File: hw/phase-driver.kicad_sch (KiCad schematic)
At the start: 13 parts, among them IC401 SN74AHCT1G125DRLR, IC402 SN74AHCT1G125DRLR, IC403 SN74AHCT1G125DRLR, Q401 MMBF170, Q402 MMBF170, Q403 MMBF170

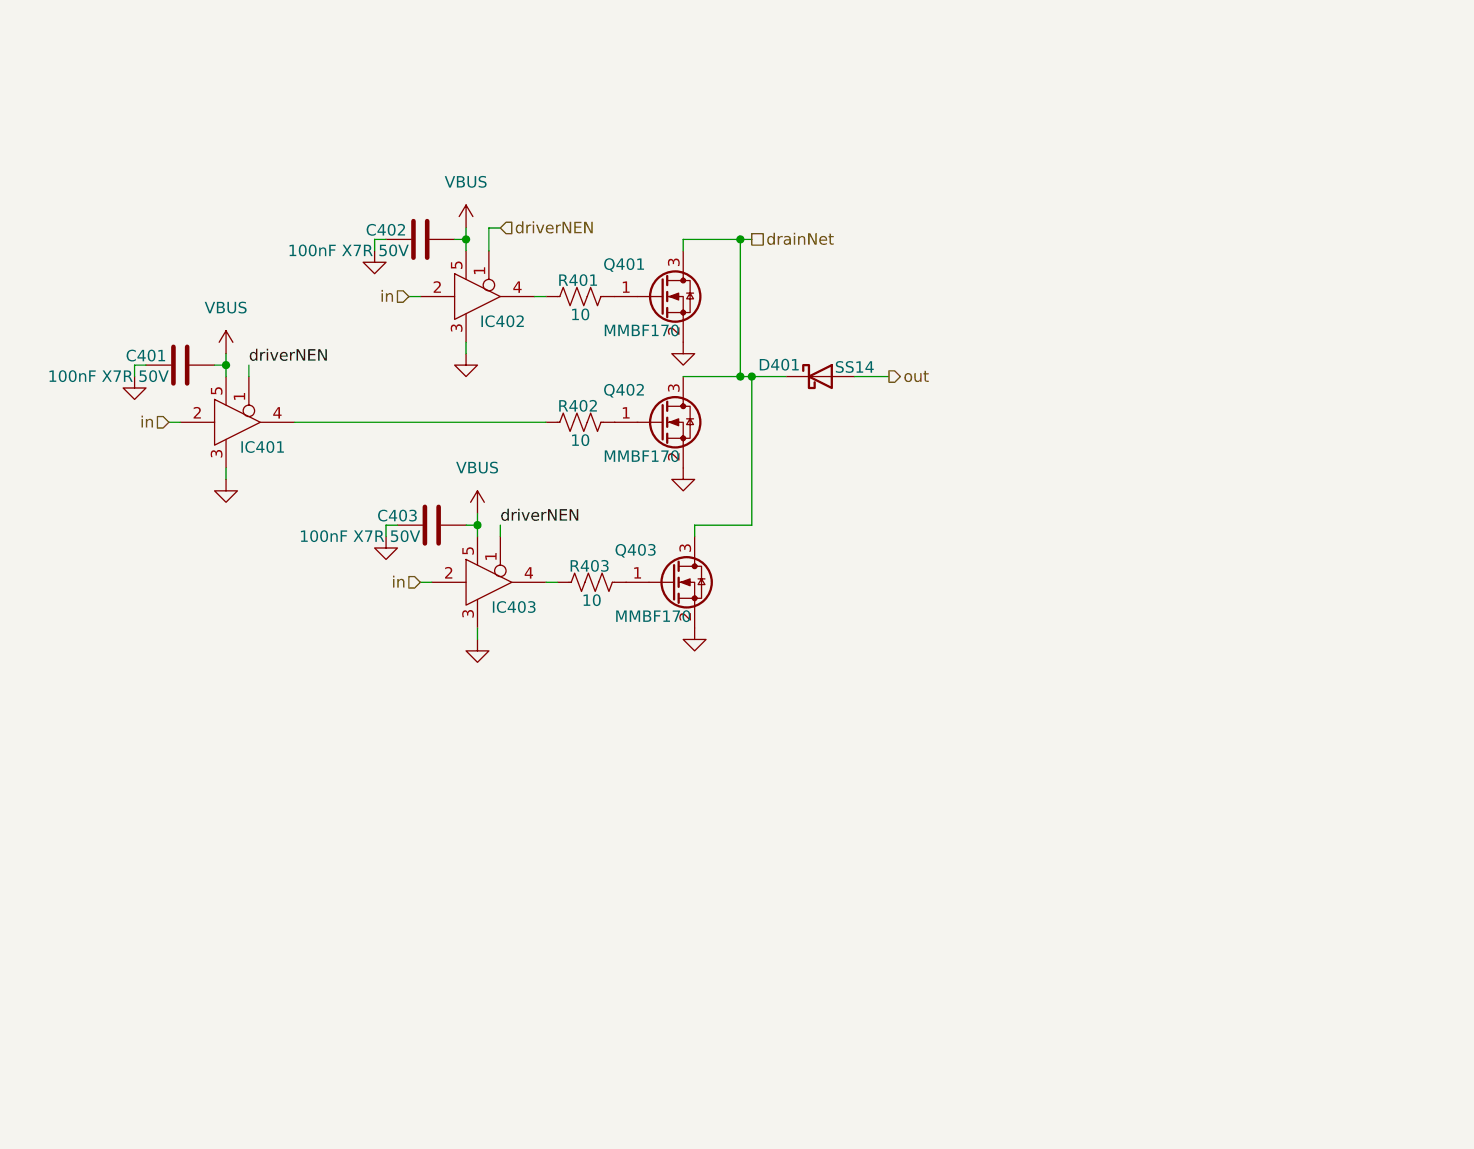
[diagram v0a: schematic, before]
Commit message: Use VFPGAIO for pullup for driverNEN. Fix some layout issues with more equal routing lengths in critical tx phase paths.
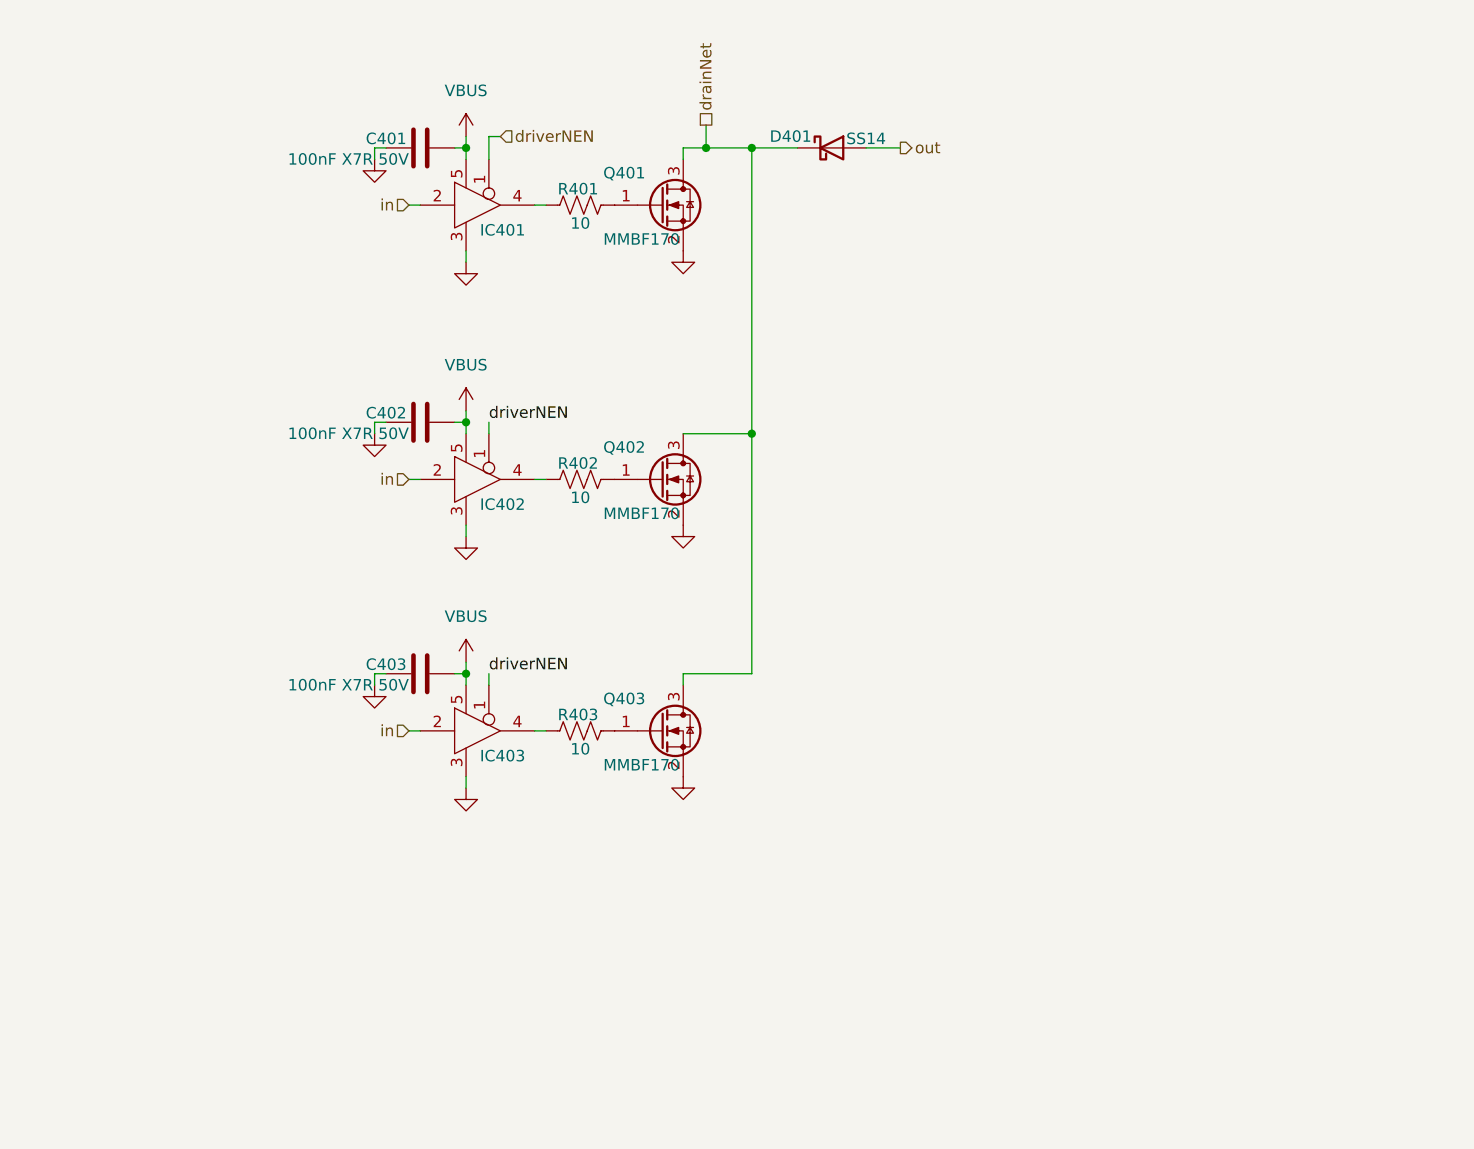
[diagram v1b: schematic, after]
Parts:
- renumbered C402 to C401, C401 to C402, IC402 to IC401, IC401 to IC402
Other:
- moved on the sheet: C401, C402, C403, D401, IC401, IC402, IC403, Q401, Q402, Q403, R401, R402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

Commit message: Fucking USB 16-pin footprint! Also, completely redid the layout and wiring of the transmitter using a MOSFET gate and R+diode gate drive, simplify BOM, enhance LPFs for square wave output >= 10MHz.
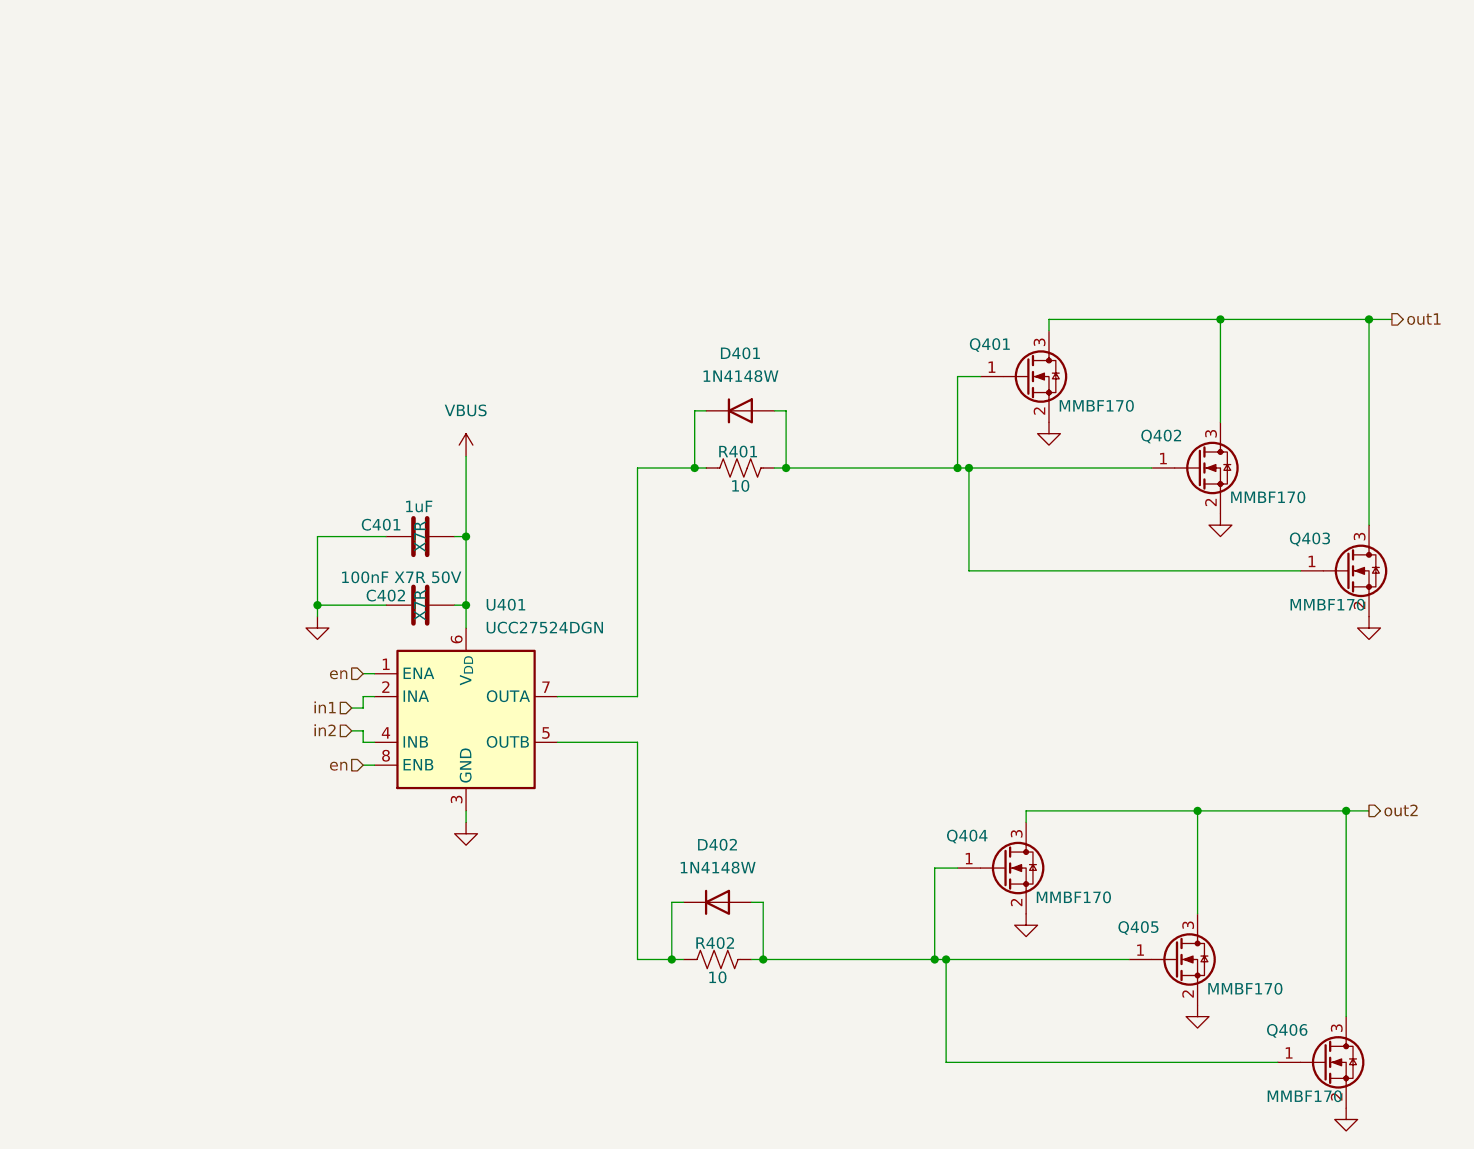
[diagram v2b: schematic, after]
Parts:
- removed C403: 100nF X7R 50V, Capacitor_SMD:C_0603_1608Metric, symbol Device:C
- removed D401: SS14, Diode_SMD:D_SMA, symbol Diode:SS14
- removed IC401, IC402, IC403: SN74AHCT1G125DRLR, Library:SOTFL50P160X60-5N, symbol Library:SN74AHCT1G125DRLR
- removed R403: 10, Resistor_SMD:R_0603_1608Metric, symbol Device:R_US
- added D401, D402: 1N4148W, Diode_SMD:D_SOD-123, symbol Diode:1N4148W
- added Q404, Q405, Q406: MMBF170, Package_TO_SOT_SMD:SOT-23, symbol Transistor_FET:BS170F
- added U401: UCC27524DGN, Package_SO:Texas_DGN0008G_VSSOP-8-1EP_3x3mm_P0.65mm_EP2x2.94mm_Mask1.846x2.15mm_ThermalVias, symbol Driver_FET:UCC27524DGN
- C401: value 100nF X7R 50V -> 1uF; footprint Capacitor_SMD:C_0603_1608Metric -> Capacitor_SMD:C_0402_1005Metric; LCSC C24452 -> C14445; LCSC_PN (none) -> C301928; MFG Kyocera AVX -> muRata; MPN KGM15BR71H104KT -> GRM155Z71A105KE1D; Manufacturer (none) -> Murata; Mouser_PN 581-KGM15BR71H104KT -> 81-GRM155Z71A105KE1D; cap-type (none) -> X7R; working-voltage (none) -> 10V
- C402: cap-type (none) -> X7R; working-voltage (none) -> 50V
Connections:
- net GND: now also Q404.2 (S), Q405.2 (S), Q406.2 (S), U401.3 (GND), U401.9 (GND)
- net VBUS: now also U401.6 (V_{DD})
- net at Q401.1 (G), R401.2: now also Q402.1 (G), Q403.1 (G), D401.2 (A)
- net at R401.1: now also D401.1 (K), U401.7 (OUTA)
- net at R402.1: now also D402.1 (K), U401.5 (OUTB)
- net at R402.2: now also D402.2 (A), Q404.1 (G), Q405.1 (G), Q406.1 (G); no longer Q402.1 (G)
- net drainNet renamed out1
- new net en: U401.1 (ENA), U401.8 (ENB)
- new net in1: U401.2 (INA)
- new net in2: U401.4 (INB)
- new net out2: Q404.3 (D), Q405.3 (D), Q406.3 (D)
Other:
- moved on the sheet: C402, Q401, Q402, Q403, R401

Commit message: Add symbols for new components, switch to SI5351 in place of FPGA. Simplify!
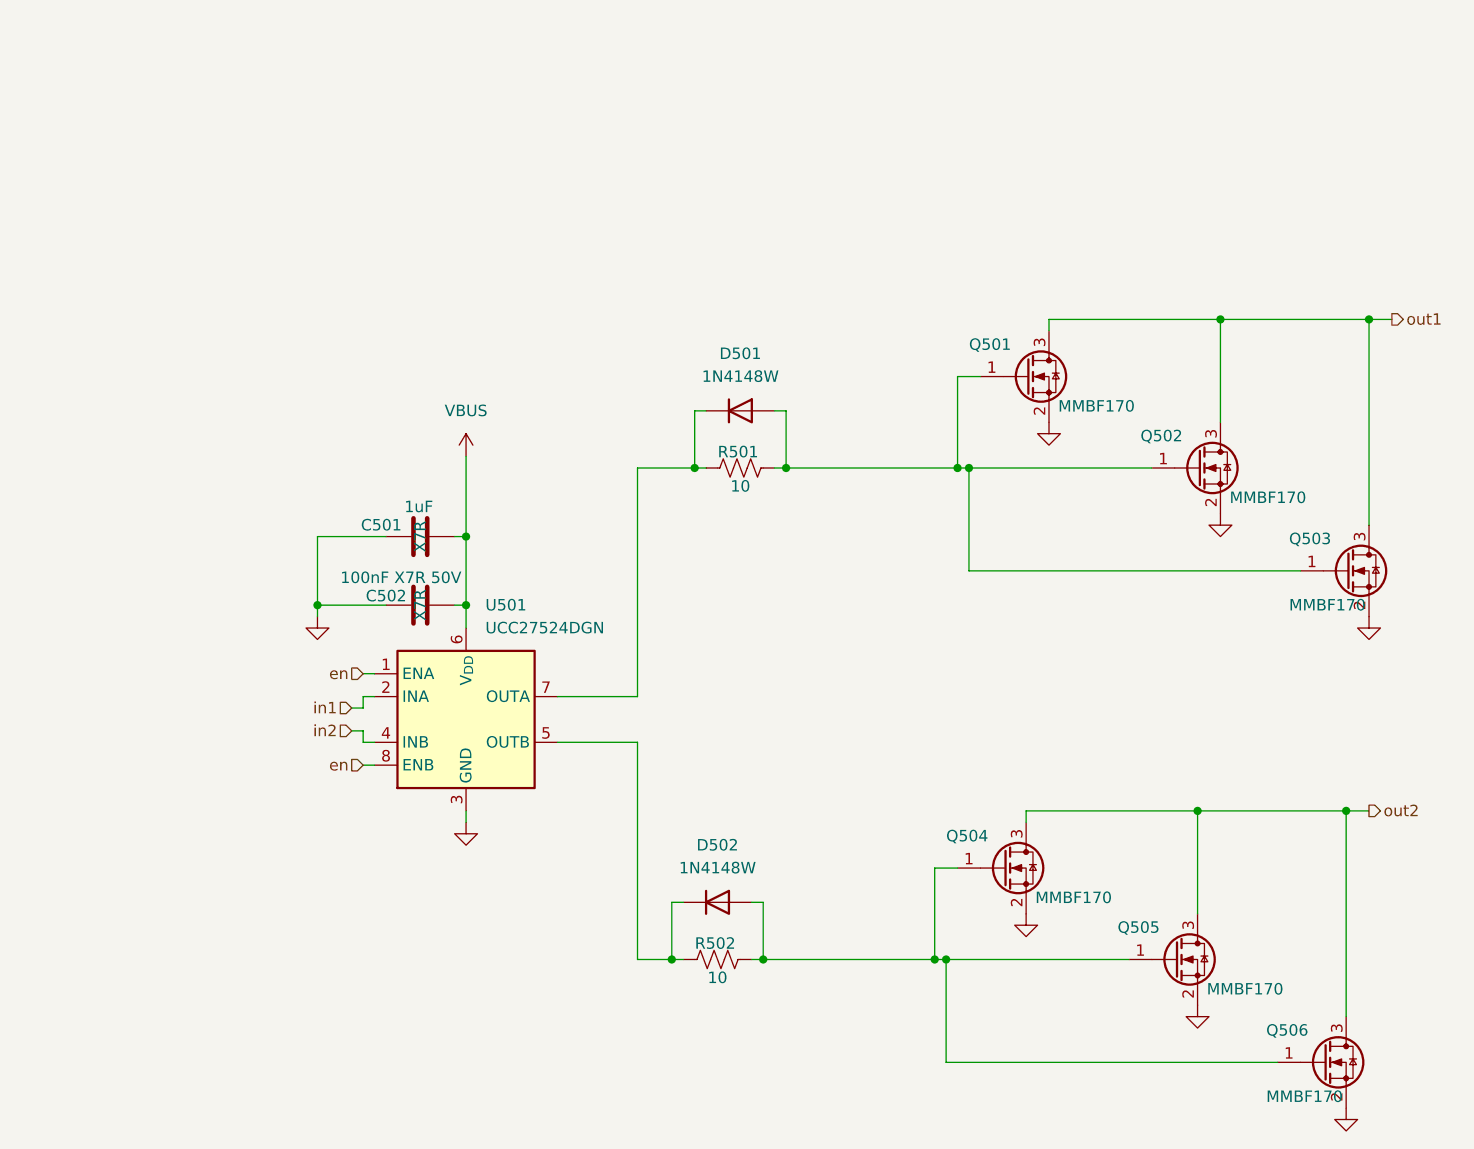
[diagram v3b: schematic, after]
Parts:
- renumbered C401 to C501, C402 to C502, D401 to D501, D402 to D502, Q401 to Q501, Q402 to Q502, Q403 to Q503, Q404 to Q504, Q405 to Q505, Q406 to Q506, R401 to R501, R402 to R502, U401 to U501
